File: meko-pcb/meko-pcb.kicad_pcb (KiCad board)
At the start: 4 copper layers, 37 x 69 mm, 143 parts, among them IC2 TPS7A2033PDBVR, IC4 TAD5212IRGER, IC5 AS5600-ASOM, J1 USB_C_Receptacle_USB2.0_16P, J2 MEM2090-00-145-00-A, J3 GDEY0154D67, J4 Conn_ARM_SWD_TagConnect_TC203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, M1 HD-EMB1204-SM, Q1 SS8050, Q2 Si1308EDL, SW1 SW_Push, SW2 SW_Push, SW3 SW_Push, SW4 SW_Push, SW5 SW_Push, SW6 SW_Push, SW7 SW_Push, SW8 SW_Push, U1 nPM1300-QEXX, U2 nRF5340-QKxx, Y1 32MHz, Y2 32.768 kHz

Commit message: small chnages
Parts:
- removed SW8: SW_Push, Button_Switch_SMD:SW_Push_SPST_NO_Alps_SKRK
- removed U1: nPM1300-QEXX, Package_DFN_QFN:QFN-32-1EP_5x5mm_P0.5mm_EP3.6x3.6mm_ThermalVias
- added SW9: SW_Push, Button_Switch_SMD:SW_Push_SPST_NO_Alps_SKRK, F.Cu at (34.0, 67.5)
- added U3: nPM1300-CAXX, PCM_nordic-lib-kicad-npm:BGA-35_7x5_3.077x2.3775mm, F.Cu at (79.4, 65.9)
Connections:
- net Net-(U2-ANT) renamed /ANT
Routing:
- net REG-OUT: track 0.00 -> 2.69 mm
- net Net-(D11-K): track 0.00 -> 2.67 mm
- net VBUSIN: track 0.00 -> 2.52 mm
- net Net-(D16-K): track 0.00 -> 1.94 mm
- net GND: track 0.00 -> 1.85 mm, vias 0 -> 1
- net +BATT: track 0.00 -> 1.78 mm
- net +3V3: track 0.00 -> 1.75 mm, vias 0 -> 2
- net /I2C_SCL: track 0.00 -> 1.34 mm
- net /I2C_SDA: track 0.00 -> 1.23 mm
- net Net-(U3-VSET2): track 0.00 -> 1.14 mm
- net /PMIC_GPIO1: track 0.00 -> 1.04 mm
- net Net-(U3-SW2): track 0.00 -> 0.60 mm
- net Net-(U3-SW1): track 0.00 -> 0.55 mm
- net /PMIC_GPIO2: vias 0 -> 1
- removed copper zone on In1.Cu, net GND
- removed copper zone on In2.Cu, net GND
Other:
- copper layers 4 -> 6

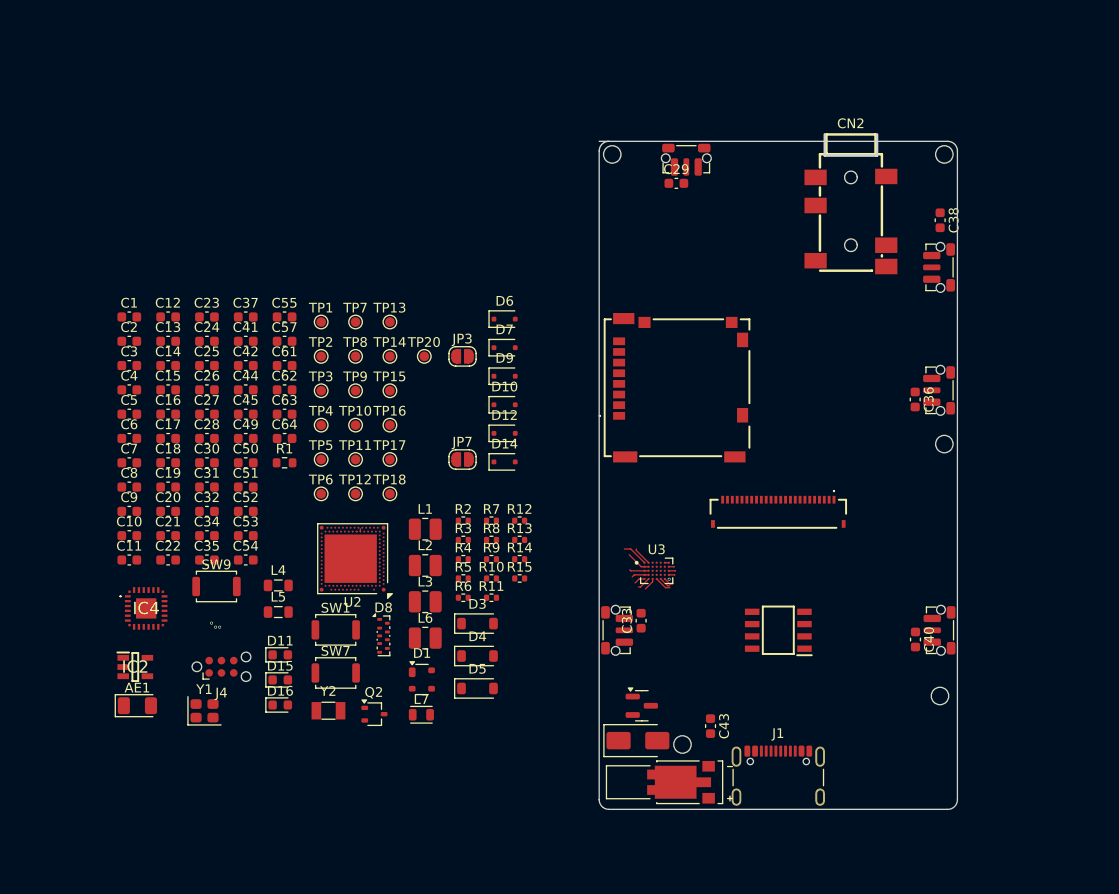
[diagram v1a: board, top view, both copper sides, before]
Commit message: added a bumch of testpoints/jumpers, fixed dac i2c adress pin
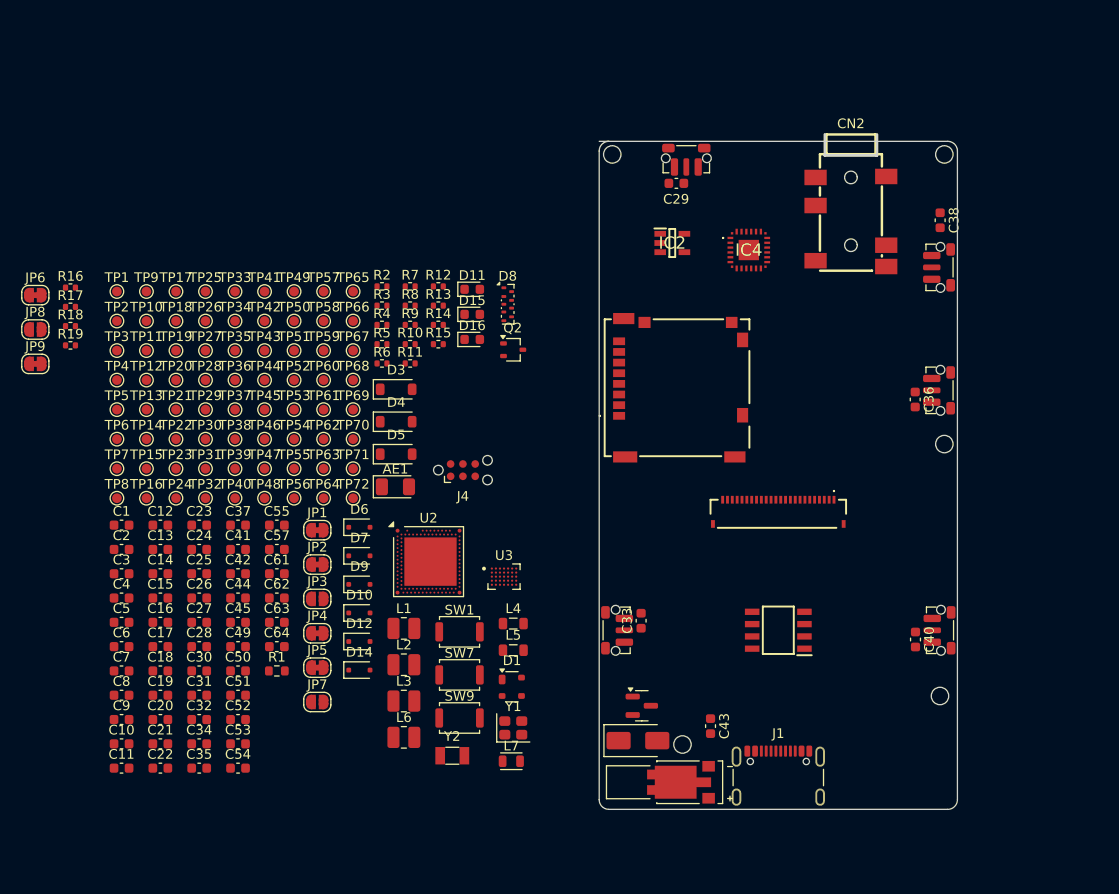
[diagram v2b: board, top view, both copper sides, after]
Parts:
- added JP1: SolderJumper_2_Bridged, Jumper:SolderJumper-2_P1.3mm_Bridged_RoundedPad1.0x1.5mm, F.Cu at (44.4, 61.7)
- added JP2: SolderJumper_2_Bridged, Jumper:SolderJumper-2_P1.3mm_Bridged_RoundedPad1.0x1.5mm, F.Cu at (44.4, 65.2)
- added JP4: SolderJumper_2_Bridged, Jumper:SolderJumper-2_P1.3mm_Bridged_RoundedPad1.0x1.5mm, F.Cu at (44.4, 72.3)
- added JP5: SolderJumper_2_Bridged, Jumper:SolderJumper-2_P1.3mm_Bridged_RoundedPad1.0x1.5mm, F.Cu at (44.4, 75.9)
- added JP6: SolderJumper_2_Bridged, Jumper:SolderJumper-2_P1.3mm_Bridged_RoundedPad1.0x1.5mm, F.Cu at (15.3, 37.4)
- added JP8: SolderJumper_2_Open, Jumper:SolderJumper-2_P1.3mm_Open_RoundedPad1.0x1.5mm, F.Cu at (15.3, 40.9)
- added JP9: SolderJumper_2_Bridged, Jumper:SolderJumper-2_P1.3mm_Bridged_RoundedPad1.0x1.5mm, F.Cu at (15.3, 44.5)
- added R16: 1k, Resistor_SMD:R_0402_1005Metric, F.Cu at (18.9, 36.6)
- added R17: 1k, Resistor_SMD:R_0402_1005Metric, F.Cu at (18.9, 38.6)
- added R18: 10k, Resistor_SMD:R_0402_1005Metric, F.Cu at (18.9, 40.6)
- added R19: 10k, Resistor_SMD:R_0402_1005Metric, F.Cu at (18.9, 42.6)
- added TP19: DISPL_SCL, TestPoint:TestPoint_Pad_D1.0mm, F.Cu at (29.8, 43.1)
- added TP21: DISPL_SDA, TestPoint:TestPoint_Pad_D1.0mm, F.Cu at (29.8, 49.2)
- added TP22: DISPL_SDA, TestPoint:TestPoint_Pad_D1.0mm, F.Cu at (29.8, 52.3)
- added TP23: DISPL_SCL, TestPoint:TestPoint_Pad_D1.0mm, F.Cu at (29.8, 55.3)
- added TP24: DISPL_SDA, TestPoint:TestPoint_Pad_D1.0mm, F.Cu at (29.8, 58.4)
- added TP25: DISPL_SDA, TestPoint:TestPoint_Pad_D1.0mm, F.Cu at (32.8, 37.0)
- added TP26: DISPL_SCL, TestPoint:TestPoint_Pad_D1.0mm, F.Cu at (32.8, 40.1)
- added TP27: DISPL_SDA, TestPoint:TestPoint_Pad_D1.0mm, F.Cu at (32.8, 43.1)
- added TP28: DISPL_SDA, TestPoint:TestPoint_Pad_D1.0mm, F.Cu at (32.8, 46.2)
- added TP29: DISPL_SCL, TestPoint:TestPoint_Pad_D1.0mm, F.Cu at (32.8, 49.2)
- added TP30: DISPL_SDA, TestPoint:TestPoint_Pad_D1.0mm, F.Cu at (32.8, 52.3)
- added TP31: DISPL_SDA, TestPoint:TestPoint_Pad_D1.0mm, F.Cu at (32.8, 55.3)
- added TP32: DISPL_SCL, TestPoint:TestPoint_Pad_D1.0mm, F.Cu at (32.8, 58.4)
- added TP33: DISPL_SDA, TestPoint:TestPoint_Pad_D1.0mm, F.Cu at (35.9, 37.0)
- added TP34: DISPL_SDA, TestPoint:TestPoint_Pad_D1.0mm, F.Cu at (35.9, 40.1)
- added TP35: DISPL_SCL, TestPoint:TestPoint_Pad_D1.0mm, F.Cu at (35.9, 43.1)
- added TP36: DISPL_SDA, TestPoint:TestPoint_Pad_D1.0mm, F.Cu at (35.9, 46.2)
- added TP37: DISPL_SDA, TestPoint:TestPoint_Pad_D1.0mm, F.Cu at (35.9, 49.2)
- added TP38: DISPL_SCL, TestPoint:TestPoint_Pad_D1.0mm, F.Cu at (35.9, 52.3)
- added TP39: DISPL_SDA, TestPoint:TestPoint_Pad_D1.0mm, F.Cu at (35.9, 55.3)
- added TP40: DISPL_SDA, TestPoint:TestPoint_Pad_D1.0mm, F.Cu at (35.9, 58.4)
- added TP41: DISPL_SCL, TestPoint:TestPoint_Pad_D1.0mm, F.Cu at (38.9, 37.0)
- added TP42: DISPL_SDA, TestPoint:TestPoint_Pad_D1.0mm, F.Cu at (38.9, 40.1)
- added TP43: DISPL_SDA, TestPoint:TestPoint_Pad_D1.0mm, F.Cu at (38.9, 43.1)
- added TP44: DISPL_SDA, TestPoint:TestPoint_Pad_D1.0mm, F.Cu at (38.9, 46.2)
- added TP45: DISPL_SDA, TestPoint:TestPoint_Pad_D1.0mm, F.Cu at (38.9, 49.2)
- added TP46: DISPL_SCL, TestPoint:TestPoint_Pad_D1.0mm, F.Cu at (38.9, 52.3)
- added TP47: DISPL_SDA, TestPoint:TestPoint_Pad_D1.0mm, F.Cu at (38.9, 55.3)
- added TP48: DISPL_SDA, TestPoint:TestPoint_Pad_D1.0mm, F.Cu at (38.9, 58.4)
- added TP49: DISPL_SCL, TestPoint:TestPoint_Pad_D1.0mm, F.Cu at (42.0, 37.0)
- added TP50: DISPL_SDA, TestPoint:TestPoint_Pad_D1.0mm, F.Cu at (42.0, 40.1)
- added TP51: DISPL_SDA, TestPoint:TestPoint_Pad_D1.0mm, F.Cu at (42.0, 43.1)
- added TP52: DISPL_SCL, TestPoint:TestPoint_Pad_D1.0mm, F.Cu at (42.0, 46.2)
- added TP53: DISPL_SDA, TestPoint:TestPoint_Pad_D1.0mm, F.Cu at (42.0, 49.2)
- added TP54: DISPL_SDA, TestPoint:TestPoint_Pad_D1.0mm, F.Cu at (42.0, 52.3)
- added TP55: DISPL_SDA, TestPoint:TestPoint_Pad_D1.0mm, F.Cu at (42.0, 55.3)
- added TP56: DISPL_SDA, TestPoint:TestPoint_Pad_D1.0mm, F.Cu at (42.0, 58.4)
- added TP57: DISPL_SDA, TestPoint:TestPoint_Pad_D1.0mm, F.Cu at (45.0, 37.0)
- added TP58: DISPL_SDA, TestPoint:TestPoint_Pad_D1.0mm, F.Cu at (45.0, 40.1)
- added TP59: DISPL_SDA, TestPoint:TestPoint_Pad_D1.0mm, F.Cu at (45.0, 43.1)
- added TP60: DISPL_SDA, TestPoint:TestPoint_Pad_D1.0mm, F.Cu at (45.0, 46.2)
- added TP61: DISPL_SDA, TestPoint:TestPoint_Pad_D1.0mm, F.Cu at (45.0, 49.2)
- added TP62: DISPL_SDA, TestPoint:TestPoint_Pad_D1.0mm, F.Cu at (45.0, 52.3)
- added TP63: DISPL_SCL, TestPoint:TestPoint_Pad_D1.0mm, F.Cu at (45.0, 55.3)
- added TP64: DISPL_SDA, TestPoint:TestPoint_Pad_D1.0mm, F.Cu at (45.0, 58.4)
- added TP65: DISPL_SCL, TestPoint:TestPoint_Pad_D1.0mm, F.Cu at (48.1, 37.0)
- added TP66: DISPL_SDA, TestPoint:TestPoint_Pad_D1.0mm, F.Cu at (48.1, 40.1)
- added TP67: DISPL_SDA, TestPoint:TestPoint_Pad_D1.0mm, F.Cu at (48.1, 43.1)
- added TP68: DISPL_SDA, TestPoint:TestPoint_Pad_D1.0mm, F.Cu at (48.1, 46.2)
- added TP69: DISPL_SDA, TestPoint:TestPoint_Pad_D1.0mm, F.Cu at (48.1, 49.2)
- added TP70: DISPL_SDA, TestPoint:TestPoint_Pad_D1.0mm, F.Cu at (48.1, 52.3)
- added TP71: DISPL_SDA, TestPoint:TestPoint_Pad_D1.0mm, F.Cu at (48.1, 55.3)
- added TP72: DISPL_SDA, TestPoint:TestPoint_Pad_D1.0mm, F.Cu at (48.1, 58.4)
- TP18, TP20: value DISPL_SDA -> DISPL_SCL
- TP9: value DISPL_SCL -> DISPL_SDA
- moved IC4 72.4 mm to (89.0, 32.7)
- moved IC2 70.7 mm to (81.0, 32.0)
- moved D11 42.7 mm to (60.4, 36.8)
- moved D16 42.7 mm to (60.4, 42.0)
- moved D15 42.7 mm to (60.4, 39.4)
- moved Q2 40.3 mm to (64.6, 43.0)
- moved D8 36.6 mm to (64.0, 38.3)
- moved AE1 34.9 mm to (52.5, 57.2)
- moved J4 32.2 mm to (59.4, 55.5)
- moved Y1 31.9 mm to (64.6, 82.1)
- moved JP3 29.2 mm to (44.4, 68.8)
- moved JP7 29.2 mm to (44.4, 79.4)
- moved TP7 28.9 mm to (23.7, 55.3)
- moved TP8 28.7 mm to (23.7, 58.4)
- moved SW9 28.5 mm to (59.1, 81.1)
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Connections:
- C44 pad 2: +3V3 -> Net-(IC4-IOVDD)
- C45 pad 2: +3V3 -> Net-(JP1-A)
- C49 pad 2: +3V3 -> /DISPL_PWR
- IC2 pad 3: /PWR_EN3V3AVCC -> Net-(IC2-EN)
- IC4 pad 6: +3V3 -> Net-(IC4-IOVDD)
- J3 pad 15: +3V3 -> /DISPL_PWR
- J3 pad 16: +3V3 -> /DISPL_PWR
- JP3 pad 2: /PWR_EN3V3AVCC -> Net-(IC2-EN)
- L7 pad 1: +3V3 -> Net-(JP1-A)
- TP10 pad 1: /DISPL_SDA -> /DISPL_TSDA
- TP18 pad 1: Net-(U2-P0.31) -> /BTN_VOL_UP
- TP20 pad 1: Net-(U2-P1.11) -> /DISPL_RESET
- TP9 pad 1: /DISPL_SCL -> /DISPL_TSDA
- U2 pad B24: /AUDIO_ADDR -> Net-(U2-P0.30)
- U3 pad E2: GND -> Net-(JP5-B)
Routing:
- net REG-OUT: track 2.69 -> 0.00 mm
- net Net-(D11-K): track 2.67 -> 0.00 mm
- net VBUSIN: track 2.52 -> 0.00 mm
- net Net-(D16-K): track 1.94 -> 0.00 mm
- net GND: track 1.85 -> 0.00 mm, vias 1 -> 0
- net +BATT: track 1.78 -> 0.00 mm
- net +3V3: track 1.75 -> 0.00 mm, vias 2 -> 0
- net /I2C_SCL: track 1.34 -> 0.00 mm
- net /I2C_SDA: track 1.23 -> 0.00 mm
- net Net-(U3-VSET2): track 1.14 -> 0.00 mm
- net /PMIC_GPIO1: track 1.04 -> 0.00 mm
- net Net-(U3-SW2): track 0.60 -> 0.00 mm
- net Net-(U3-SW1): track 0.55 -> 0.00 mm
- net /PMIC_GPIO2: track 0.30 -> 0.00 mm, vias 1 -> 0
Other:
- copper layers 6 -> 4

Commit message: changed parts that are not avalibile on lcsc
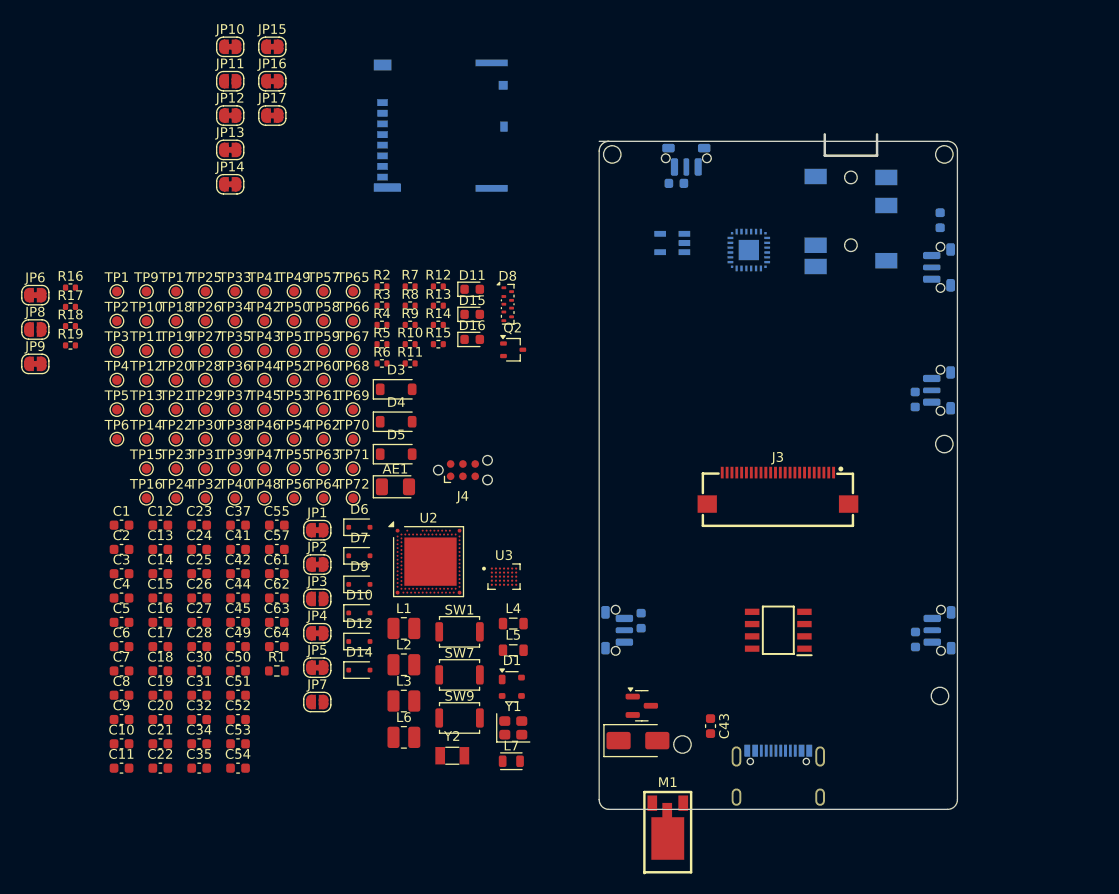
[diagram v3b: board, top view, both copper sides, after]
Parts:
- removed J2: MEM2090-00-145-00-A, MEM2090-00-145-00-A:MEM20900014500A
- removed TP7: SDA, TestPoint:TestPoint_Pad_D1.0mm
- removed TP8: SCL, TestPoint:TestPoint_Pad_D1.0mm
- added J5: 503398-1892, 503398-1892:5033981892, B.Cu at (49.7, 13.3)
- added JP10: SolderJumper_2_Bridged, Jumper:SolderJumper-2_P1.3mm_Bridged_RoundedPad1.0x1.5mm, F.Cu at (35.4, 11.7)
- added JP11: SolderJumper_2_Open, Jumper:SolderJumper-2_P1.3mm_Open_RoundedPad1.0x1.5mm, F.Cu at (35.4, 15.3)
- added JP12: SolderJumper_2_Bridged, Jumper:SolderJumper-2_P1.3mm_Bridged_RoundedPad1.0x1.5mm, F.Cu at (35.4, 18.8)
- added JP13: SolderJumper_2_Bridged, Jumper:SolderJumper-2_P1.3mm_Bridged_RoundedPad1.0x1.5mm, F.Cu at (35.4, 22.4)
- added JP14: SolderJumper_2_Bridged, Jumper:SolderJumper-2_P1.3mm_Bridged_RoundedPad1.0x1.5mm, F.Cu at (35.4, 25.9)
- added JP15: SolderJumper_2_Bridged, Jumper:SolderJumper-2_P1.3mm_Bridged_RoundedPad1.0x1.5mm, F.Cu at (39.7, 11.7)
- added JP16: SolderJumper_2_Bridged, Jumper:SolderJumper-2_P1.3mm_Bridged_RoundedPad1.0x1.5mm, F.Cu at (39.7, 15.3)
- added JP17: SolderJumper_2_Bridged, Jumper:SolderJumper-2_P1.3mm_Bridged_RoundedPad1.0x1.5mm, F.Cu at (39.7, 18.8)
- C29, C33, C36, C38, C40, CN2, IC2, IC4, SW2, SW3, SW4, SW5, SW6: moved to B.Cu
- J1: footprint Connector_USB:USB_C_Receptacle_GCT_USB4105-xx-A_16P_TopMnt_Horizontal -> Connector_USB:USB_C_Receptacle_G-Switch_GT-USB-7010ASV; moved to B.Cu
- J3: footprint FH34SRJ-24S-0.5SH(99):FH34SRJ24S05SH99-disp -> FPC-SMD_24P-P0.50_FPC-05FB-24PH20:FPC-SMD_24P-P0.50_FPC-05FB-24PH20
- M1: value HD-EMB1204-SM -> ~; footprint HD-EMB1204-SM:PUI_HD-EMB1204-SM -> LD-SM-430:SMD_LD-SM-430-1
- moved M1 4.27 mm to (80.6, 91.3), turned to 0 degrees
- moved J3 2.63 mm to (92.0, 57.3)
- turned J1 to 180 degrees
- turned C29 to 180 degrees
- turned CN2 to 180 degrees
- turned IC2 to 180 degrees
- turned IC4 to 180 degrees
- turned SW2 to 0 degrees
- turned SW3 to 90 degrees
- turned SW4 to -90 degrees
- turned SW5 to -90 degrees
- turned SW6 to -90 degrees
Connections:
- net /BCLK renamed /AUDIO_BCLK
- net /DIN renamed /AUDIO_DIN
- net /DOUT renamed /AUDIO_DOUT
- net /FSYNC renamed /AUDIO_FSYNC
- net /LED renamed Net-(U2-DCX/TRACECLK/P0.12)
- net /PMIC_GPIO5 renamed Net-(U2-P0.19)
- C64 pad 1: +HALL3V3 -> Net-(IC5-VDD3V3)
- IC4 pad 7: /I2C_SCL -> Net-(IC4-SCL)
- IC4 pad 8: /I2C_SDA -> Net-(IC4-SDA)
- IC5 pad 2: +HALL3V3 -> Net-(IC5-VDD3V3)
- IC5 pad 6: /I2C_SDA -> Net-(IC5-SDA)
- IC5 pad 7: /I2C_SCL -> Net-(IC5-SCL)
- JP3 pad 1: REG-OUT -> Net-(IC2-EN)
- JP3 pad 2: Net-(IC2-EN) -> /PWR_EN3V3AVCC
- JP9 pad 1: /PWR_EN3V3AVCC -> Net-(IC2-EN)
- JP9 pad 2: Net-(IC2-EN) -> REG-OUT
- TP38 pad 1: /AUDIO_GPIO1 -> Net-(U2-AIN5/P0.26)
- TP39 pad 1: /AUDIO_GPIO2 -> Net-(U2-AIN6/P0.27)
- TP40 pad 1: /AUDIO_GPO1 -> /AUDIO_GPIO1
- TP41 pad 1: /AUDIO_GPI1 -> /AUDIO_GPIO2
- TP42 pad 1: Net-(U2-P0.30) -> /AUDIO_GPO1
- TP43 pad 1: Net-(U2-P0.31) -> /AUDIO_GPI1
- TP50 pad 1: /MEM_COM -> Net-(U2-P1.07)
- TP55 pad 1: /DISPL_~{CS} -> /MEM_LEVER
- TP56 pad 1: /DISPL_~{D/C} -> /MEM_SWITCH
- TP9 pad 1: /DISPL_TSDA -> /DISPL_TSCL
- U2 pad A17: /DISPL_~{CS} -> /MEM_LEVER
- U2 pad AE31: /AUDIO_GPO1 -> /AUDIO_GPIO1
- U2 pad AK24: /MEM_COM -> Net-(U2-P1.07)
- U2 pad AK30: /AUDIO_GPIO2 -> Net-(U2-AIN6/P0.27)
- U2 pad AL29: /AUDIO_GPIO1 -> Net-(U2-AIN5/P0.26)
- U2 pad B16: /DISPL_~{D/C} -> /MEM_SWITCH
- U2 pad B22: Net-(U2-P0.31) -> /AUDIO_GPI1
- U2 pad B24: Net-(U2-P0.30) -> /AUDIO_GPO1
- U2 pad U31: /AUDIO_GPI1 -> /AUDIO_GPIO2
- U3 pad E3: /I2C_SCL -> Net-(JP17-B)
- U3 pad E5: /I2C_SDA -> Net-(JP16-B)

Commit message: fixed edge cuts
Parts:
- moved M1 4.08 mm to (78.4, 87.9), turned to 90 degrees
- moved CN2 0.75 mm to (99.7, 30.5)
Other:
- outline, holes or cut-outs redrawn
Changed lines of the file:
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@@
 	(footprint "LD-SM-430:SMD_LD-SM-430-1"
 		(layer "F.Cu")
-		(at 80.580967 91.316217)
+		(at 78.4265 87.8525 90)
 		(property "Reference" "M1"
-			(at -0.000967 -3.588933 0)
+			(at -0.000967 -3.588933 90)
 			(layer "F.SilkS")
 			(effects
@@
 		)
 		(property "Value" "~"
-			(at -0.000967 6.6015 0)
+			(at -0.000967 6.6015 90)
 			(layer "F.Fab")
 			(effects
@@
 		)
 		(property "Datasheet" "https://item.szlcsc.com/datasheet/LD-SM-430/43080312.html"
-			(at 0 0 0)
+			(at 0 0 90)
 			(layer "F.Fab")
 			(hide yes)
@@
 		)
 		(property "Description" ""
-			(at 0 0 0)
+			(at 0 0 90)
 			(layer "F.Fab")
 			(hide yes)
@@
 		)
 		(property "Manufacturer Part" "LD-SM-430"
-			(at 0 0 0)
+			(at 0 0 90)
 			(unlocked yes)
 			(layer "F.Fab")
@@
 		)
 		(property "Manufacturer" "LEADER(立得)"
-			(at 0 0 0)
+			(at 0 0 90)
 			(unlocked yes)
 			(layer "F.Fab")
@@
 		)
 		(property "Supplier Part" "C41348533"
-			(at 0 0 0)
+			(at 0 0 90)
 			(unlocked yes)
 			(layer "F.Fab")
@@
 		)
 		(property "Supplier" "LCSC"
-			(at 0 0 0)
+			(at 0 0 90)
 			(unlocked yes)
 			(layer "F.Fab")
@@
 		)
 		(property "LCSC Part Name" "LD-SM-430"
-			(at 0 0 0)
+			(at 0 0 90)
 			(unlocked yes)
 			(layer "F.Fab")
@@
 		(sheetfile "meko-pcb.kicad_sch")
 		(fp_line
-			(start -2.413 -2.6075)
-			(end 2.413 -2.6075)
+			(start 2.413 -2.6075)
+			(end 2.413 5.683)
 			(stroke
 				(width 0.254)
@@
 		)
 		(fp_line
-			(start -2.413 5.683)
-			(end 2.413 5.683)
+			(start -2.413 -2.6075)
+			(end 2.413 -2.6075)
 			(stroke
 				(width 0.254)
@@
 		)
 		(fp_line
-			(start -2.413 5.7745)
-			(end -2.413 -2.6075)
+			(start -2.413 5.683)
+			(end 2.413 5.683)
 			(stroke
 				(width 0.254)
@@
 		)
 		(fp_line
-			(start 2.413 -2.6075)
-			(end 2.413 5.683)
+			(start -2.413 5.7745)
+			(end -2.413 -2.6075)
 			(stroke
 				(width 0.254)
@@
 		)
 		(fp_line
-			(start -2.286 -2.5585)
-			(end 2.314 -2.5585)
+			(start 2.314 -2.5585)
+			(end 2.286 5.461)
 			(stroke
 				(width 0.051)
@@
 		)
 		(fp_line
-			(start -2.286 5.461)
-			(end -2.286 -2.5585)
+			(start -2.286 -2.5585)
+			(end 2.314 -2.5585)
 			(stroke
 				(width 0.051)
@@
 		)
 		(fp_line
-			(start 2.314 -2.5585)
-			(end 2.286 5.461)
+			(start -2.286 5.461)
+			(end -2.286 -2.5585)
 			(stroke
 				(width 0.051)
@@
 		(fp_poly
 			(pts
-				(xy -2.1 -2.2565) (xy -2.1 -0.6565) (xy -1.1 -0.6565) (xy -1.1 -2.2565)
+				(xy 1.1 -2.2565) (xy 1.1 -0.6565) (xy 2.1 -0.6565) (xy 2.1 -2.2565)
 			)
 			(stroke
@@
 		(fp_poly
 			(pts
-				(xy 1.1 -2.2565) (xy 1.1 -0.6565) (xy 2.1 -0.6565) (xy 2.1 -2.2565)
+				(xy -2.1 -2.2565) (xy -2.1 -0.6565) (xy -1.1 -0.6565) (xy -1.1 -2.2565)
 			)
 			(stroke
@@
 		)
 		(fp_text user "${REFERENCE}"
-			(at 0 0 0)
+			(at 0 0 90)
 			(layer "F.Fab")
 			(effects
@@
 		)
 		(pad "1" smd custom
-			(at -1.6 -1.4565)
+			(at -1.6 -1.4565 90)
 			(size 0.000001 0.000001)
 			(layers "F.Cu" "F.Mask" "F.Paste")
@@
 		)
 		(pad "2" smd custom
-			(at 1.6 -1.4565)
+			(at 1.6 -1.4565 90)
 			(size 0.000001 0.000001)
 			(layers "F.Cu" "F.Mask" "F.Paste")
@@
 		)
 		(pad "3" smd custom
-			(at 0 1.4565)
+			(at 0 1.4565 90)
 			(size 0.000001 0.000001)
 			(layers "F.Cu" "F.Mask" "F.Paste")
@@
 	(footprint "PJ-242:AUDIO-SMD_PJ-342"
 		(layer "B.Cu")
-		(at 99.5 29.7795 180)
+		(at 99.68 30.5025 180)
 		(property "Reference" "CN2"
 			(at 0 10.102 0)
@@
 			(layer "Dwgs.User")
 		)
-		(fp_line
-			(start 2.7 6.8)
-			(end 2.7 9)
-			(stroke
-				(width 0.254)
-				(type default)
-			)
-			(layer "Edge.Cuts")
-		)
-		(fp_line
-			(start 2.6 6.8)
-			(end 2.7 6.8)
-			(stroke
-				(width 0.254)
-				(type default)
-			)
-			(layer "Edge.Cuts")
-		)
-		(fp_line
+		(fp_rect
 			(start -2.7 9)
-			(end -2.7 6.9)
-			(stroke
-				(width 0.254)
-				(type default)
-			)
-			(layer "Edge.Cuts")
-		)
-		(fp_line
-			(start -2.7 6.9)
-			(end -2.7 6.8)
-			(stroke
-				(width 0.254)
-				(type default)
-			)
-			(layer "Edge.Cuts")
-		)
-		(fp_line
-			(start -2.7 6.8)
-			(end 2.6 6.8)
+			(end 2.7 6.8)
 			(stroke
-				(width 0.254)
+				(width 0.05)
 				(type default)
 			)
+			(fill no)
 			(layer "Edge.Cuts")
 		)
@@
 	(gr_line
 		(start 110.5 22.5)
-		(end 110.5 89.5)
+		(end 110.5 89.5125)
 		(stroke
 			(width 0.05)
@@
 	)
 	(gr_line
-		(start 73.5 21.5)
+		(start 74.5 21.5)
 		(end 109.5 21.5)
 		(stroke
